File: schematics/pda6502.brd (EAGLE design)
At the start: 100 x 80 mm, 35 parts, among them IC1 74HC00D, IC2 74HC138D, IC3 DS1813-SMD, J1 CON_HEADER_2X07-PTH, U1 W65C02S, U2 W65C22S, U3 28C256, U4 UM61256AK-12

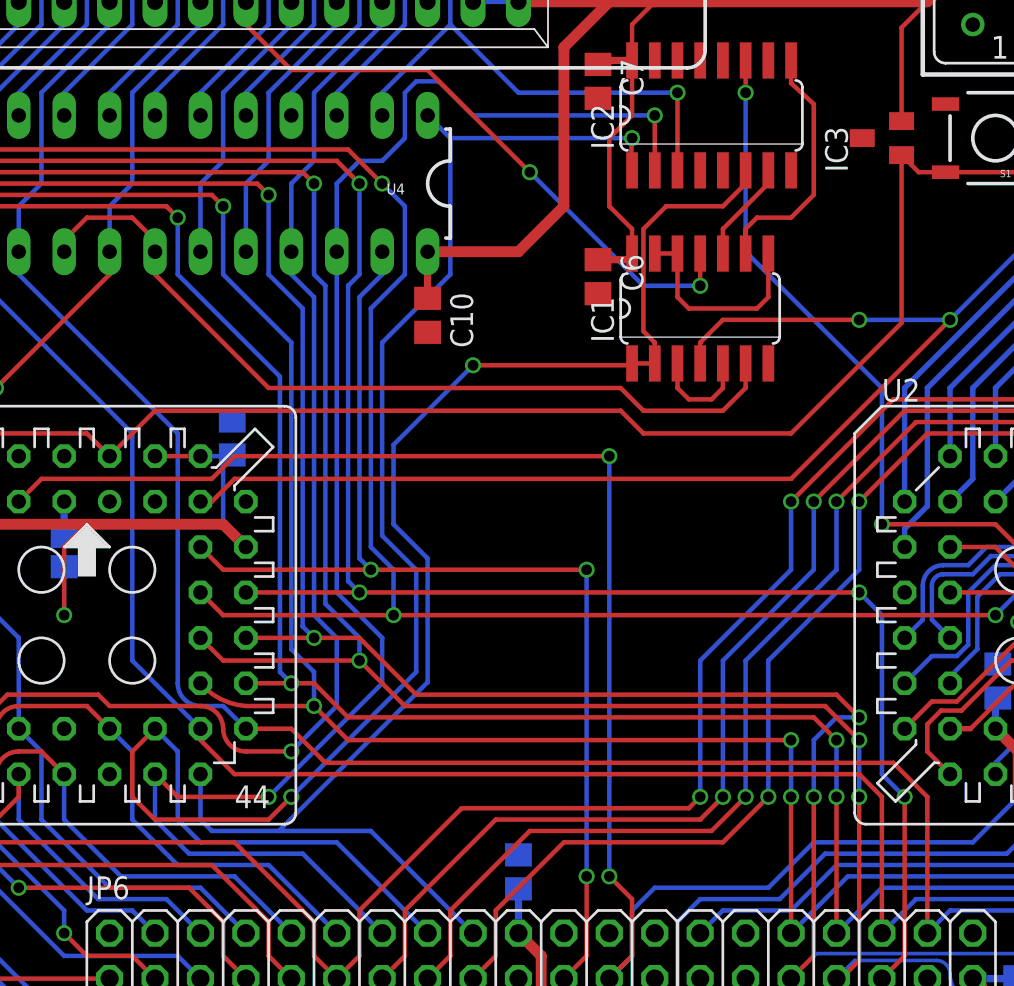
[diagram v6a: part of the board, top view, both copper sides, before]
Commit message: board: expanded GND pour around 74HC chips; 1 airwire remaining.
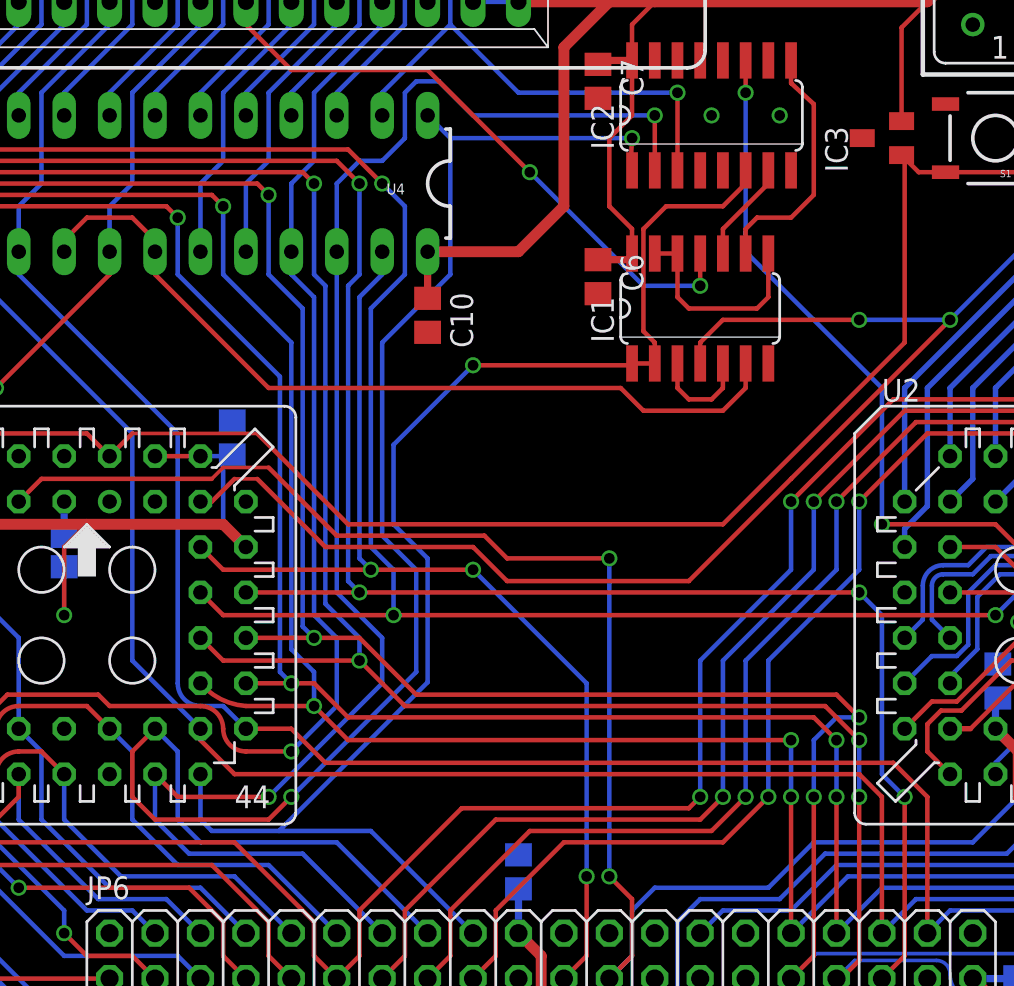
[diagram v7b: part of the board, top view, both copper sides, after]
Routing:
- net PHI2: track 162.8 -> 167.5 mm
- net RESB: track 146.6 -> 150.7 mm
- net IRQB: track 97.2 -> 93.4 mm
- net RWB: track 101.3 -> 97.6 mm
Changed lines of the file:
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@@
 </polygon>
 <contactref element="C14" pad="1"/>
-<wire x1="67.48" y1="52.07" x2="72.136" y2="53.975" width="0" layer="19" extent="1-1"/>
-<wire x1="63.5" y1="50.2666" x2="67.48" y2="52.07" width="0" layer="19" extent="1-1"/>
+<via x="59.055" y="53.34" extent="1-16" drill="0.6"/>
+<via x="62.865" y="53.34" extent="1-16" drill="0.6"/>
 <wire x1="97.57" y1="69.85" x2="95.25" y2="60.96" width="0" layer="19" extent="1-1"/>
 </signal>
@@
 <wire x1="39.37" y1="28.575" x2="40.005" y2="27.94" width="0.254" layer="16"/>
 <wire x1="31.75" y1="27.94" x2="30.48" y2="29.21" width="0.254" layer="1"/>
-<wire x1="40.005" y1="27.94" x2="52.07" y2="27.94" width="0.254" layer="1"/>
+<wire x1="40.005" y1="27.94" x2="45.72" y2="27.94" width="0.254" layer="1"/>
 <wire x1="58.42" y1="9.525" x2="62.865" y2="9.525" width="0.254" layer="16"/>
 <wire x1="62.865" y1="9.525" x2="65.405" y2="12.065" width="0.254" layer="16"/>
@@
 <wire x1="56.515" y1="3.81" x2="52.07" y2="3.81" width="0.254" layer="16"/>
 <wire x1="52.07" y1="3.81" x2="50.8" y2="5.08" width="0.254" layer="16"/>
-<via x="52.07" y="27.94" extent="1-16" drill="0.6"/>
-<wire x1="52.07" y1="27.94" x2="52.07" y2="10.795" width="0.254" layer="16"/>
+<via x="45.72" y="27.94" extent="1-16" drill="0.6"/>
+<wire x1="45.72" y1="27.94" x2="52.07" y2="21.59" width="0.254" layer="16"/>
+<wire x1="52.07" y1="21.59" x2="52.07" y2="10.795" width="0.254" layer="16"/>
 </signal>
 <signal name="ROM_CE">
@@
 <wire x1="12.065" y1="27.305" x2="12.065" y2="32.385" width="0.254" layer="16"/>
 <wire x1="12.065" y1="32.385" x2="15.24" y2="35.56" width="0.254" layer="16"/>
-<wire x1="25.4" y1="34.29" x2="27.94" y2="36.83" width="0.254" layer="1"/>
-<wire x1="27.94" y1="36.83" x2="53.975" y2="36.83" width="0.254" layer="1"/>
-<wire x1="53.975" y1="36.83" x2="55.245" y2="35.56" width="0.254" layer="1"/>
-<wire x1="55.245" y1="35.56" x2="63.5" y2="35.56" width="0.254" layer="1"/>
-<wire x1="63.5" y1="35.56" x2="69.68" y2="41.74" width="0.254" layer="1"/>
-<wire x1="69.68" y1="41.74" x2="69.68" y2="51.12" width="0.254" layer="1"/>
+<wire x1="25.4" y1="34.29" x2="26.67" y2="35.56" width="0.254" layer="1"/>
 <wire x1="69.68" y1="51.12" x2="70.635" y2="50.165" width="0.254" layer="1"/>
 <wire x1="70.635" y1="50.165" x2="72.136" y2="50.165" width="0.254" layer="1"/>
+<wire x1="26.67" y1="35.56" x2="33.655" y2="35.56" width="0.2032" layer="1"/>
+<wire x1="33.655" y1="35.56" x2="38.735" y2="30.48" width="0.254" layer="1"/>
+<wire x1="38.735" y1="30.48" x2="59.69" y2="30.48" width="0.254" layer="1"/>
+<wire x1="59.69" y1="30.48" x2="69.85" y2="40.64" width="0.254" layer="1"/>
+<wire x1="69.85" y1="40.64" x2="69.85" y2="50.95" width="0.254" layer="1"/>
+<wire x1="69.85" y1="50.95" x2="69.68" y2="51.12" width="0.2032" layer="1"/>
 </signal>
 <signal name="PHI2">
@@
 <via x="72.39" y="41.91" extent="1-16" drill="0.6"/>
 <wire x1="72.39" y1="41.91" x2="63.5" y2="33.02" width="0.254" layer="1"/>
-<wire x1="63.5" y1="33.02" x2="32.385" y2="33.02" width="0.254" layer="1"/>
 <wire x1="82.55" y1="19.05" x2="81.28" y2="17.78" width="0.254" layer="16"/>
 <wire x1="81.28" y1="17.78" x2="81.28" y2="13.97" width="0.254" layer="16"/>
@@
 <wire x1="30.48" y1="31.75" x2="31.115" y2="31.75" width="0.254" layer="1"/>
 <wire x1="31.115" y1="31.75" x2="32.385" y2="33.02" width="0.254" layer="1"/>
+<wire x1="32.385" y1="33.02" x2="33.655" y2="33.02" width="0.2032" layer="1"/>
+<wire x1="33.655" y1="33.02" x2="37.465" y2="29.21" width="0.254" layer="1"/>
+<wire x1="37.465" y1="29.21" x2="45.72" y2="29.21" width="0.254" layer="1"/>
+<wire x1="45.72" y1="29.21" x2="47.625" y2="27.305" width="0.254" layer="1"/>
+<wire x1="47.625" y1="27.305" x2="57.785" y2="27.305" width="0.254" layer="1"/>
+<wire x1="57.785" y1="27.305" x2="63.5" y2="33.02" width="0.254" layer="1"/>
 </signal>
 <signal name="N$1">
@@
 <wire x1="20.32" y1="31.75" x2="21.59" y2="33.02" width="0.254" layer="1"/>
 <wire x1="21.59" y1="33.02" x2="31.115" y2="33.02" width="0.254" layer="1"/>
-<wire x1="32.385" y1="34.29" x2="53.34" y2="34.29" width="0.254" layer="1"/>
 <wire x1="64.77" y1="12.7" x2="73.66" y2="12.7" width="0.254" layer="16"/>
 <wire x1="73.66" y1="12.7" x2="76.2" y2="15.24" width="0.254" layer="16"/>
@@
 <wire x1="54.61" y1="6.35" x2="53.34" y2="5.08" width="0.254" layer="16"/>
 <via x="53.34" y="10.795" extent="1-16" drill="0.6"/>
-<wire x1="32.385" y1="34.29" x2="31.115" y2="33.02" width="0.254" layer="1"/>
-<via x="53.34" y="34.29" extent="1-16" drill="0.6"/>
-<wire x1="53.34" y1="34.29" x2="53.34" y2="10.795" width="0.254" layer="16"/>
+<via x="53.34" y="28.575" extent="1-16" drill="0.6"/>
+<wire x1="53.34" y1="28.575" x2="53.34" y2="10.795" width="0.254" layer="16"/>
+<wire x1="31.115" y1="33.02" x2="31.75" y2="33.655" width="0.2032" layer="1"/>
+<wire x1="31.75" y1="33.655" x2="34.29" y2="33.655" width="0.2032" layer="1"/>
+<wire x1="34.29" y1="33.655" x2="38.1" y2="29.845" width="0.254" layer="1"/>
+<wire x1="38.1" y1="29.845" x2="46.355" y2="29.845" width="0.254" layer="1"/>
+<wire x1="46.355" y1="29.845" x2="47.625" y2="28.575" width="0.254" layer="1"/>
+<wire x1="47.625" y1="28.575" x2="53.34" y2="28.575" width="0.254" layer="1"/>
 </signal>
 <signal name="N$9">

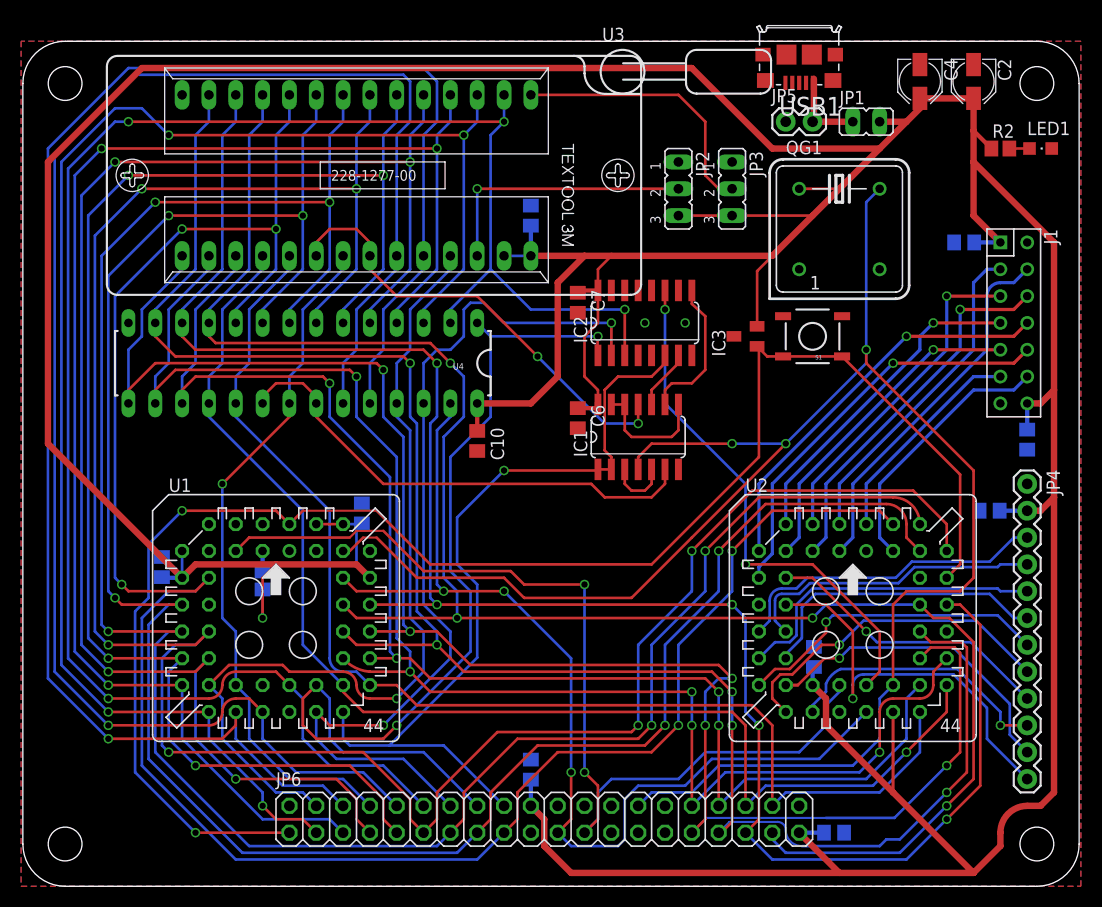
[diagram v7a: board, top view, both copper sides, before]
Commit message: board: main power re-routed; more ground plane. 0 airwires!
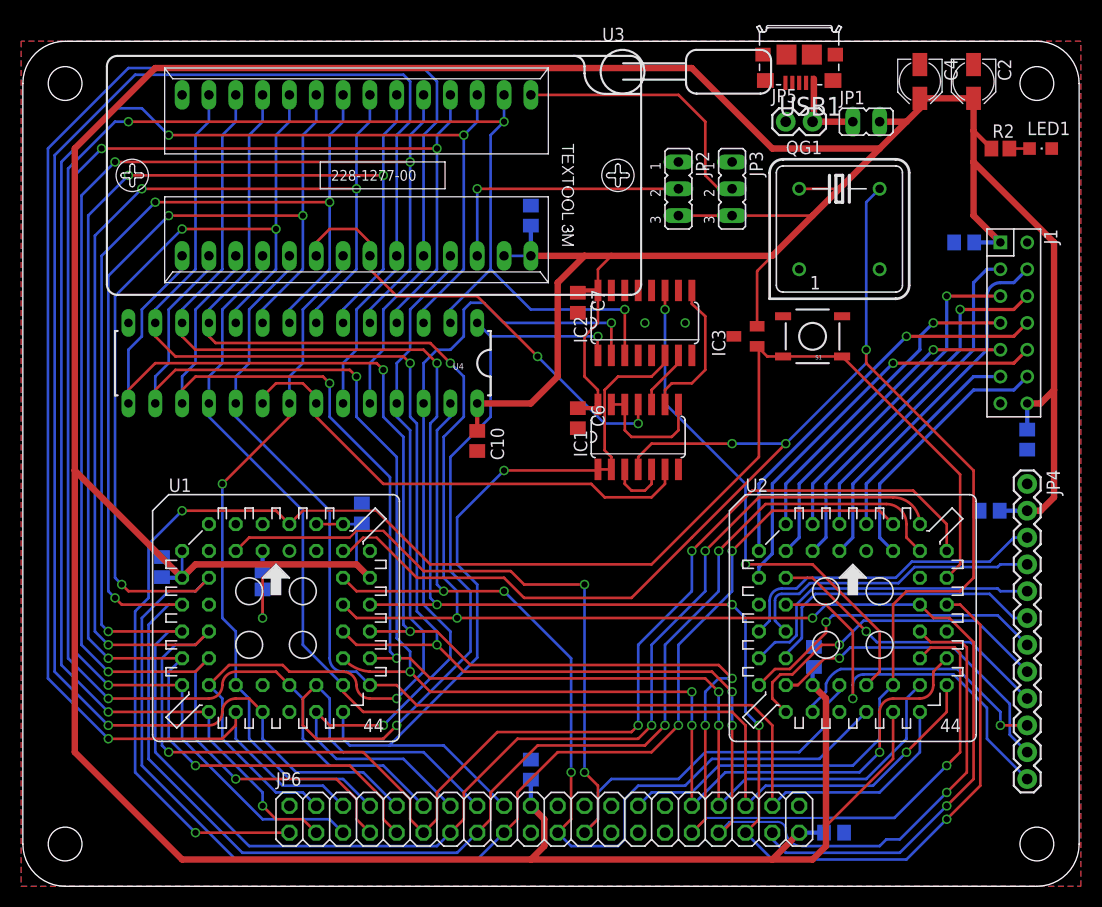
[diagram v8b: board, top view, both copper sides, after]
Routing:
- net 5V: track 491.4 -> 507.4 mm
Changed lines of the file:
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@@
 <via x="59.055" y="53.34" extent="1-16" drill="0.6"/>
 <via x="62.865" y="53.34" extent="1-16" drill="0.6"/>
-<wire x1="97.57" y1="69.85" x2="95.25" y2="60.96" width="0" layer="19" extent="1-1"/>
 </signal>
 <signal name="5V">
@@
 <wire x1="97.79" y1="46.99" x2="97.79" y2="60.96" width="0.6096" layer="1"/>
 <wire x1="97.79" y1="60.96" x2="90.17" y2="68.58" width="0.6096" layer="1"/>
-<wire x1="73.66" y1="5.08" x2="77.47" y2="1.27" width="0.6096" layer="1"/>
-<wire x1="77.47" y1="1.27" x2="90.17" y2="1.27" width="0.6096" layer="1"/>
-<wire x1="97.79" y1="8.89" x2="97.79" y2="36.83" width="0.6096" layer="1"/>
 <wire x1="97.79" y1="36.83" x2="97.79" y2="46.99" width="0.6096" layer="1"/>
-<wire x1="96.52" y1="7.62" x2="97.79" y2="8.89" width="0.6096" layer="1"/>
 <wire x1="48.26" y1="7.62" x2="49.53" y2="6.35" width="0.6096" layer="1"/>
 <wire x1="49.53" y1="6.35" x2="49.53" y2="3.81" width="0.6096" layer="1"/>
-<wire x1="49.53" y1="3.81" x2="52.07" y2="1.27" width="0.6096" layer="1"/>
-<wire x1="52.07" y1="1.27" x2="77.47" y2="1.27" width="0.6096" layer="1"/>
 <wire x1="74.93" y1="19.05" x2="76.2" y2="17.78" width="0.6096" layer="1"/>
-<wire x1="76.2" y1="17.78" x2="76.2" y2="15.24" width="0.6096" layer="1"/>
-<wire x1="82.55" y1="16.51" x2="82.55" y2="8.89" width="0.3048" layer="1"/>
-<wire x1="92.71" y1="3.81" x2="90.17" y2="1.27" width="0.6096" layer="1"/>
-<wire x1="82.55" y1="8.89" x2="90.17" y2="1.27" width="0.6096" layer="1"/>
 <wire x1="76.012" y1="5.08" x2="73.66" y2="5.08" width="0.4064" layer="16"/>
-<wire x1="76.2" y1="15.24" x2="82.55" y2="8.89" width="0.6096" layer="1"/>
 <wire x1="92.644" y1="35.56" x2="95.25" y2="35.56" width="0.4064" layer="16"/>
 <wire x1="95.25" y1="35.56" x2="96.52" y2="35.56" width="0.6096" layer="1"/>
 <wire x1="96.52" y1="35.56" x2="97.79" y2="36.83" width="0.6096" layer="1"/>
-<wire x1="92.71" y1="3.81" x2="92.71" y2="5.08" width="0.6096" layer="1"/>
-<wire x1="96.52" y1="7.62" x2="95.25" y2="7.62" width="0.6096" layer="1"/>
-<wire x1="92.71" y1="5.08" x2="95.25" y2="7.62" width="0.6096" layer="1" curve="-90"/>
 <contactref element="C14" pad="2"/>
 <wire x1="48.26" y1="10.099" x2="48.26" y2="7.62" width="0.4064" layer="16"/>
@@
 <wire x1="81.28" y1="69.85" x2="71.12" y2="69.85" width="0.6096" layer="1"/>
 <wire x1="71.12" y1="69.85" x2="63.5" y2="77.47" width="0.6096" layer="1"/>
-<wire x1="63.5" y1="77.47" x2="11.43" y2="77.47" width="0.6096" layer="1"/>
-<wire x1="11.43" y1="77.47" x2="2.54" y2="68.58" width="0.6096" layer="1"/>
-<wire x1="2.54" y1="68.58" x2="2.54" y2="41.91" width="0.6096" layer="1"/>
-<wire x1="2.54" y1="41.91" x2="15.24" y2="29.21" width="0.6096" layer="1"/>
+<wire x1="63.5" y1="77.47" x2="12.7" y2="77.47" width="0.6096" layer="1"/>
+<wire x1="12.7" y1="77.47" x2="5.08" y2="69.85" width="0.6096" layer="1"/>
+<wire x1="5.08" y1="69.85" x2="5.08" y2="39.37" width="0.6096" layer="1"/>
+<wire x1="5.08" y1="39.37" x2="15.24" y2="29.21" width="0.6096" layer="1"/>
 <wire x1="30.48" y1="34.29" x2="32.319" y2="34.29" width="0.254" layer="16"/>
 <wire x1="32.319" y1="34.29" x2="32.258" y2="34.356" width="0.254" layer="16"/>
@@
 <wire x1="52.705" y1="45.273" x2="54.2646" y2="45.273" width="0.4064" layer="1"/>
 <wire x1="54.2646" y1="45.273" x2="54.61" y2="45.6184" width="0.254" layer="1"/>
+<wire x1="5.08" y1="39.37" x2="5.08" y2="12.7" width="0.6096" layer="1"/>
+<wire x1="5.08" y1="12.7" x2="15.24" y2="2.54" width="0.6096" layer="1"/>
+<wire x1="15.24" y1="2.54" x2="48.26" y2="2.54" width="0.6096" layer="1"/>
+<wire x1="48.26" y1="2.54" x2="49.53" y2="3.81" width="0.6096" layer="1"/>
+<wire x1="48.26" y1="2.54" x2="71.12" y2="2.54" width="0.6096" layer="1"/>
+<wire x1="71.12" y1="2.54" x2="73.66" y2="5.08" width="0.6096" layer="1"/>
+<wire x1="71.12" y1="2.54" x2="74.93" y2="2.54" width="0.6096" layer="1"/>
+<wire x1="74.93" y1="2.54" x2="76.2" y2="3.81" width="0.6096" layer="1"/>
+<wire x1="76.2" y1="3.81" x2="76.2" y2="5.715" width="0.6096" layer="1"/>
+<wire x1="76.2" y1="5.715" x2="76.2" y2="17.78" width="0.6096" layer="1"/>
+<wire x1="82.55" y1="16.51" x2="82.55" y2="12.065" width="0.254" layer="1"/>
+<wire x1="82.55" y1="12.065" x2="76.2" y2="5.715" width="0.254" layer="1"/>
 </signal>
 <signal name="PA0">
